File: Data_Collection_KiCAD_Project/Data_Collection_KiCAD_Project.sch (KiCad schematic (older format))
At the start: 4 parts

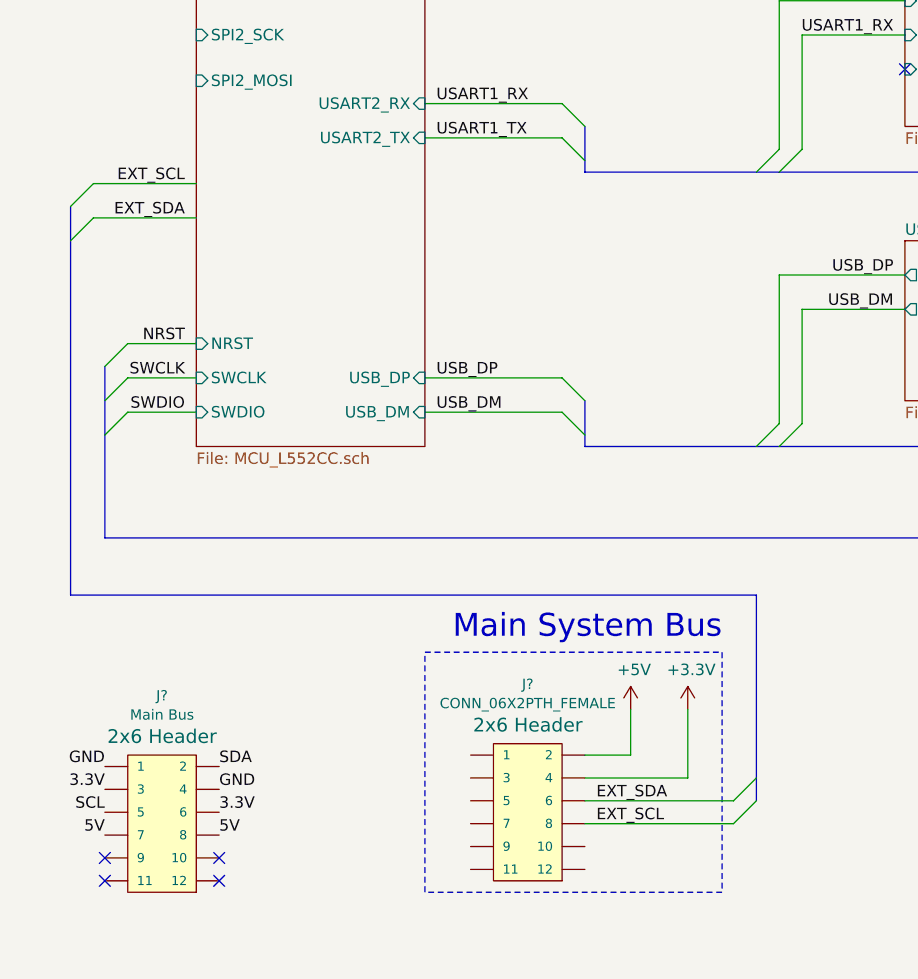
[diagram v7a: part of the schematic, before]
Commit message: Added Main Bus Layout
added main bus connector and connected various pins

TODO:
-Implement I2C interrupt pin
-Add I2C Pullups
-Add I2C Capacitors
-Check for auxiliary pins needed from sensors
-Add power buffer cap and diode?
-Double check and finalize layouts
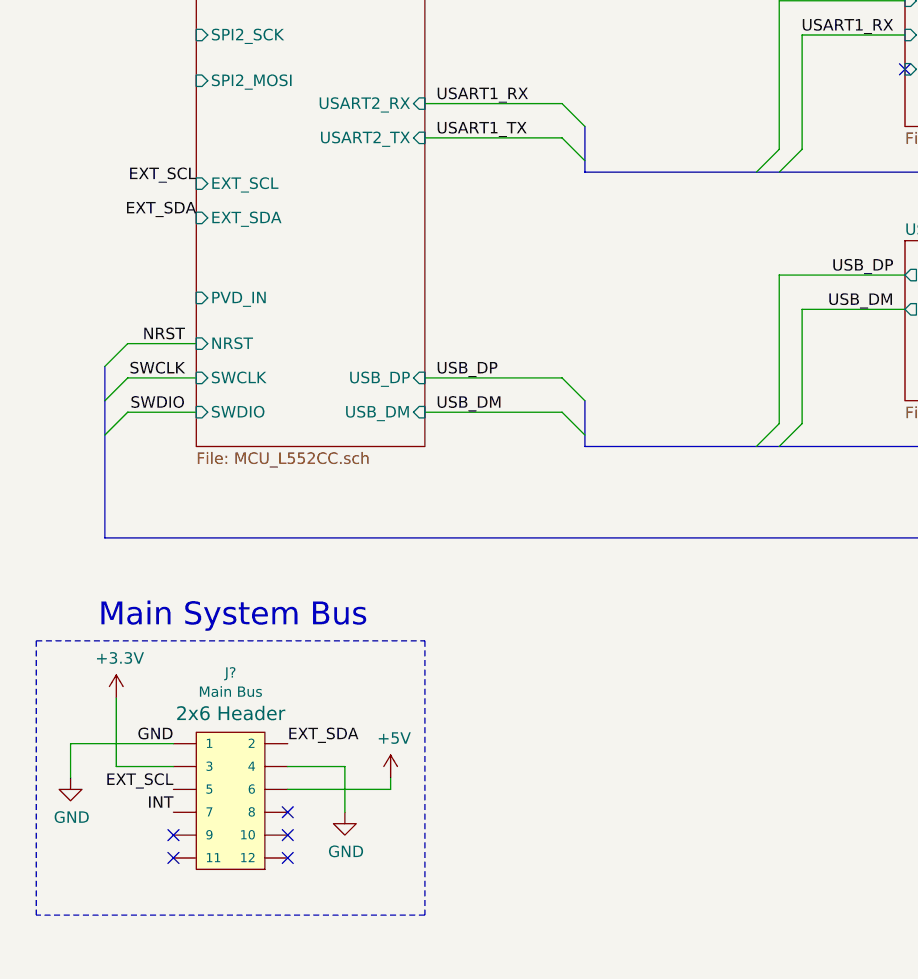
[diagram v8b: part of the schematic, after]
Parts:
- removed J?: CONN_06X2PTH_FEMALE, 2X6, symbol SparkFun-Connectors:CONN_06X2PTH_FEMALE
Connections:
- net SCL is gone; now on net EXT_SCL: J?.5
- net SDA is gone; now on net EXT_SDA: J?.2
- net +3V3: now also J?.3
- net +5V: now also J?.6
- removed net 3.3V: J?.3, J?.6
- net 5V: no longer names the net of J?.8
- net 5V: no longer J?.7
- new net INT: J?.7
- no-connect marks 9 -> 10
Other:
- moved on the sheet: J?
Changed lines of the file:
@@
 L power:+5V #PWR?
 U 1 1 61577BBB
-P 3450 6650
-F 0 "#PWR?" H 3450 6500 50  0001 C CNN
-F 1 "+5V" H 3465 6823 50  0000 C CNN
-F 2 "" H 3450 6650 50  0001 C CNN
-F 3 "" H 3450 6650 50  0001 C CNN
-	1    3450 6650
-	1    0    0    -1
-$EndComp
-Wire Wire Line
-	3450 6850 3450 6650
+P 2400 6950
+F 0 "#PWR?" H 2400 6800 50  0001 C CNN
+F 1 "+5V" H 2415 7123 50  0000 C CNN
+F 2 "" H 2400 6950 50  0001 C CNN
+F 3 "" H 2400 6950 50  0001 C CNN
+	1    2400 6950
+	1    0    0    -1
+$EndComp
 $Comp
 L power:+3.3V #PWR?
 U 1 1 61579C7C
-P 3700 6650
-F 0 "#PWR?" H 3700 6500 50  0001 C CNN
-F 1 "+3.3V" H 3715 6823 50  0000 C CNN
-F 2 "" H 3700 6650 50  0001 C CNN
-F 3 "" H 3700 6650 50  0001 C CNN
-	1    3700 6650
-	1    0    0    -1
-$EndComp
-Wire Wire Line
-	3700 6650 3700 6950
-Text Notes 3850 6350 2    100  ~ 0
+P 1200 6600
+F 0 "#PWR?" H 1200 6450 50  0001 C CNN
+F 1 "+3.3V" H 1215 6773 50  0000 C CNN
+F 2 "" H 1200 6600 50  0001 C CNN
+F 3 "" H 1200 6600 50  0001 C CNN
+	1    1200 6600
+	1    0    0    -1
+$EndComp
+Text Notes 2300 6300 2    100  ~ 0
 Main System Bus
 Text Notes 2850 1300 2    100  ~ 0
@@
 NoConn ~ 5450 6950
 NoConn ~ 5450 7050
-Wire Wire Line
-	3450 6850 3250 6850
-Wire Wire Line
-	3250 6950 3700 6950
 $Comp
 L Device:C C?
@@
 F15 "SWCLK" I L 1550 5200 50
 F16 "NRST" I L 1550 5050 50
+F17 "PVD_IN" I L 1550 4850 50
+F18 "EXT_SDA" I L 1550 4500 50
+F19 "EXT_SCL" I L 1550 4350 50
 $EndSheet
 Wire Wire Line
@@
 F5 "~CS" I R 5350 2350 50
 $EndSheet
-$Comp
-L SparkFun-Connectors:CONN_06X2PTH_FEMALE J?
-U 1 1 619BABDC
-P 3000 7100
-F 0 "J?" H 3000 7660 45  0000 C CNN
-F 1 "CONN_06X2PTH_FEMALE" H 3000 7576 45  0000 C CNN
-F 2 "2X6" H 3000 7550 20  0001 C CNN
-F 3 "" H 3000 7100 50  0001 C CNN
-F 4 "2x6 Header" H 3000 7481 60  0000 C CNN "Field4"
-	1    3000 7100
-	1    0    0    -1
-$EndComp
 Text Label 2600 1600 0    50   ~ 0
 I2C1_SDA
@@
 Text Label 5400 7150 2    50   ~ 0
 NRST
-Wire Bus Line
-	4000 6150 1000 6150
-Entry Wire Line
-	4000 7050 3900 7150
-Entry Wire Line
-	4000 6950 3900 7050
-Entry Wire Line
-	1000 4450 1100 4350
-Entry Wire Line
-	1000 4600 1100 4500
-Wire Wire Line
-	1100 4500 1550 4500
-Wire Wire Line
-	1100 4350 1550 4350
-Text Label 1500 4500 2    50   ~ 0
+Text Label 1550 4500 2    50   ~ 0
 EXT_SDA
-Text Label 1500 4350 2    50   ~ 0
+Text Label 1550 4350 2    50   ~ 0
 EXT_SCL
-Wire Wire Line
-	3250 7050 3900 7050
-Text Label 3300 7050 0    50   ~ 0
+Text Label 1950 6800 0    50   ~ 0
 EXT_SDA
-Wire Wire Line
-	3900 7150 3250 7150
-Text Label 3300 7150 0    50   ~ 0
+Text Label 1450 7000 2    50   ~ 0
 EXT_SCL
-Wire Notes Line
-	2550 6400 3850 6400
-Wire Notes Line
-	3850 6400 3850 7450
-Wire Notes Line
-	3850 7450 2550 7450
-Wire Notes Line
-	2550 7450 2550 6400
 Wire Notes Line
 	4950 6400 4950 7750
@@
 L SparkFun-Connectors:CONN_06X2PTH_FEMALE J?
 U 1 1 617A50A2
-P 1400 7150
-F 0 "J?" H 1400 7710 45  0000 C CNN
-F 1 "Main Bus" H 1400 7626 45  0000 C CNN
-F 2 "2X6" H 1400 7600 20  0001 C CNN
-F 3 "" H 1400 7150 50  0001 C CNN
-F 4 "2x6 Header" H 1400 7531 60  0000 C CNN "Field4"
-	1    1400 7150
-	1    0    0    -1
-$EndComp
-Text Label 1650 7000 0    50   ~ 0
+P 1700 7050
+F 0 "J?" H 1700 7610 45  0000 C CNN
+F 1 "Main Bus" H 1700 7526 45  0000 C CNN
+F 2 "2X6" H 1700 7500 20  0001 C CNN
+F 3 "" H 1700 7050 50  0001 C CNN
+F 4 "2x6 Header" H 1700 7431 60  0000 C CNN "Field4"
+	1    1700 7050
+	1    0    0    -1
+$EndComp
+Text Label 1450 6800 2    50   ~ 0
 GND
-Text Label 1150 6900 2    50   ~ 0
-GND
-Text Label 1150 7200 2    50   ~ 0
-5V
-Text Label 1650 7200 0    50   ~ 0
-5V
-Text Label 1650 7100 0    50   ~ 0
-3.3V
-Text Label 1150 7000 2    50   ~ 0
-3.3V
-Text Label 1650 6900 0    50   ~ 0
-SDA
-Text Label 1150 7100 2    50   ~ 0
-SCL
-NoConn ~ 1150 7300
-NoConn ~ 1150 7400
-NoConn ~ 1650 7400
-NoConn ~ 1650 7300
-Wire Bus Line
-	1000 4450 1000 6150
-Wire Bus Line
-	4000 6150 4000 7050
+NoConn ~ 1450 7200
+NoConn ~ 1450 7300
+NoConn ~ 1950 7300
+NoConn ~ 1950 7200
+NoConn ~ 1950 7100
+Text Label 1450 7100 2    50   ~ 0
+INT
+Wire Wire Line
+	1950 7000 2400 7000
+Wire Wire Line
+	2400 7000 2400 6950
+Wire Wire Line
+	1450 6900 1200 6900
+$Comp
+L power:GND #PWR?
+U 1 1 618118F6
+P 2200 7100
+F 0 "#PWR?" H 2200 6850 50  0001 C CNN
+F 1 "GND" H 2205 6927 50  0000 C CNN
+F 2 "" H 2200 7100 50  0001 C CNN
+F 3 "" H 2200 7100 50  0001 C CNN
+	1    2200 7100
+	1    0    0    -1
+$EndComp
+Wire Wire Line
+	2200 7100 2200 6900
+Wire Wire Line
+	2200 6900 1950 6900
+Wire Wire Line
+	1200 6600 1200 6900
+Wire Wire Line
+	1450 6800 1000 6800
+Wire Wire Line
+	1000 6800 1000 6950
+$Comp
+L power:GND #PWR?
+U 1 1 6181AAF8
+P 1000 6950
+F 0 "#PWR?" H 1000 6700 50  0001 C CNN
+F 1 "GND" H 1005 6777 50  0000 C CNN
+F 2 "" H 1000 6950 50  0001 C CNN
+F 3 "" H 1000 6950 50  0001 C CNN
+	1    1000 6950
+	1    0    0    -1
+$EndComp
+Wire Notes Line
+	2550 6350 2550 7550
+Wire Notes Line
+	2550 7550 850  7550
+Wire Notes Line
+	850  6350 850  7550
+Wire Notes Line
+	850  6350 2550 6350
 Wire Bus Line
 	3250 1700 3250 1900
